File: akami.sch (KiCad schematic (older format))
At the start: 66 parts, among them J1 USB_C_Receptacle_USB2.0, J2 Conn_01x01, J3 Conn_01x01, Q2 AO3401A, U1 nRF52840, U2 TP4054, U3 AP2112K-3.3, U4 ProMicro_2, Y1 32MHz, Y2 32.768 kHz

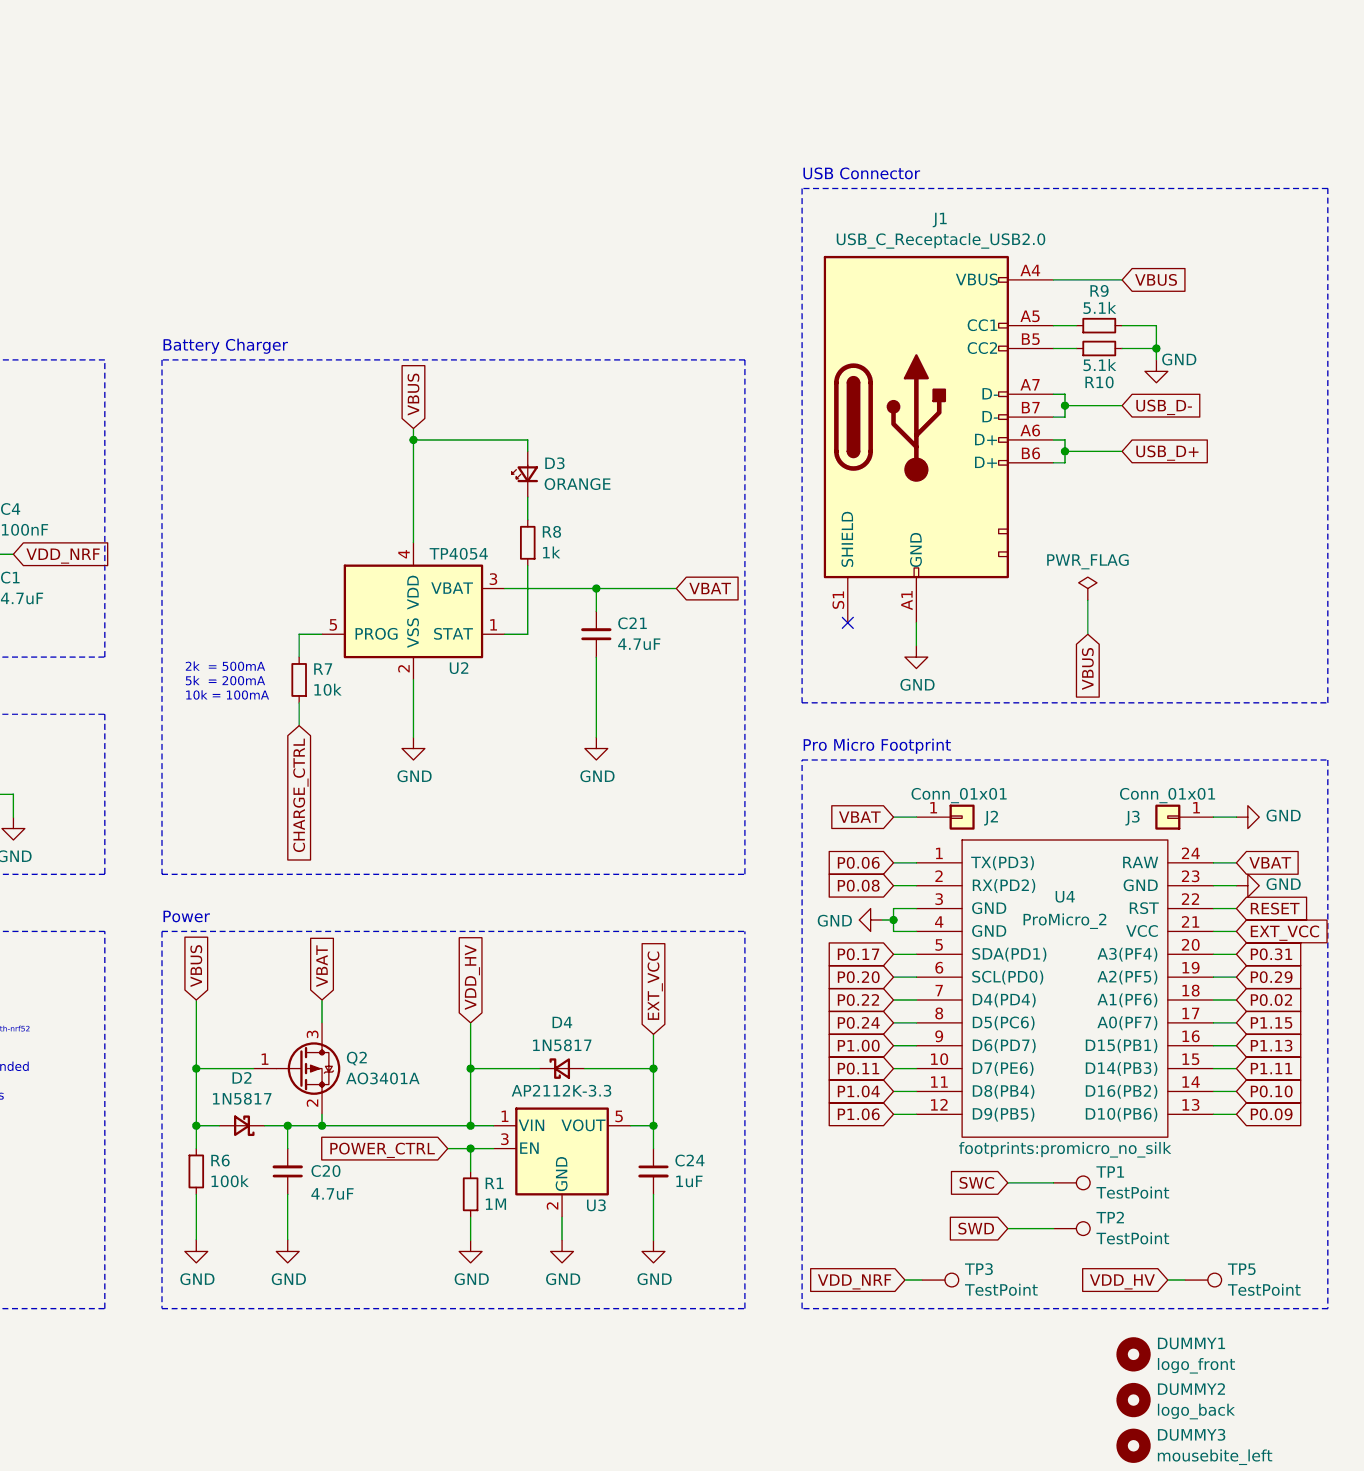
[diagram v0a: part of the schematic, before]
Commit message: rev 2.1 (hv): 1. remove the 1M pulldown on the LDO enable pin; AP2112K has an    internal pull-down already. 2. adjust pcb layout/routing slightly.
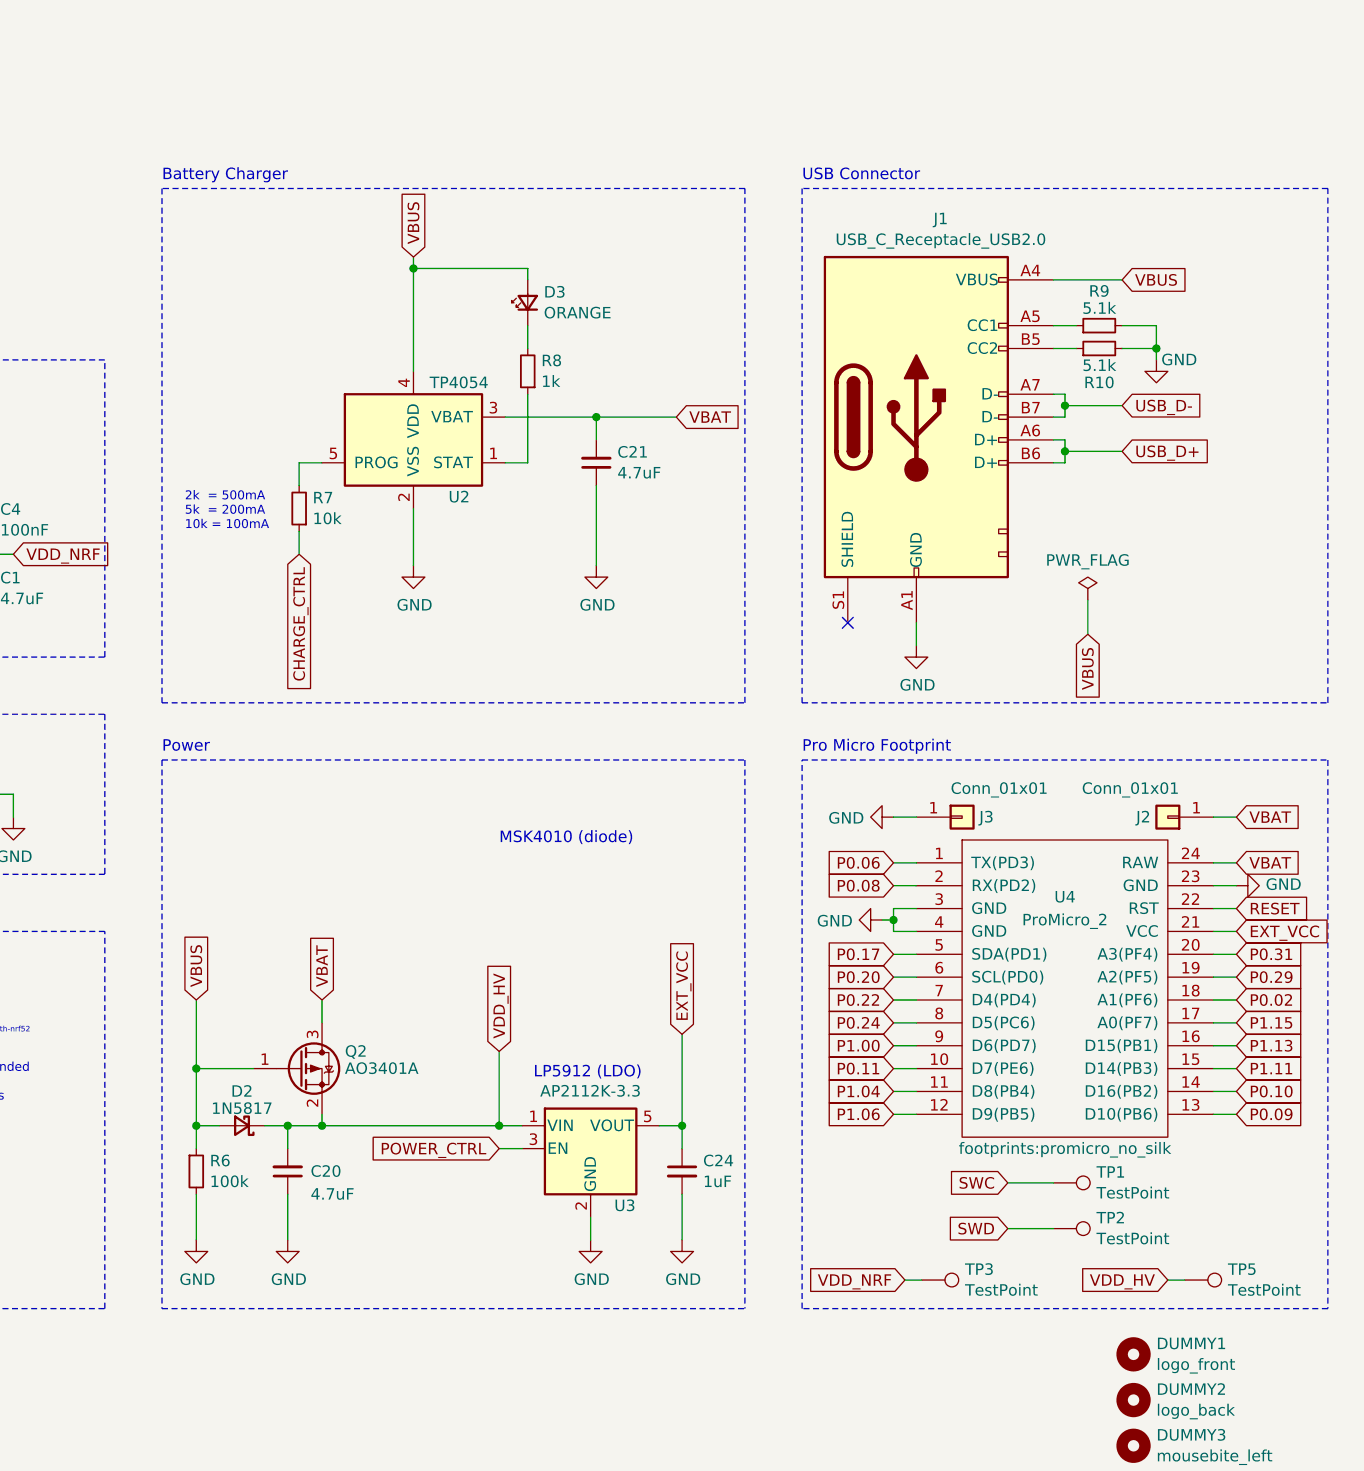
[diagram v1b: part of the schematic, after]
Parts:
- removed D4: 1N5817, Diode_SMD:D_SOD-323, symbol Device:D_Schottky_Small
- removed R1: 1M, Resistor_SMD:R_0402_1005Metric, symbol Device:R_Small
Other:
- note added: "LP5912 (LDO)"
- note added: "MSK4010 (diode)"
- moved on the sheet: C21, C24, D3, J2, J3, R7, R8, U2, U3

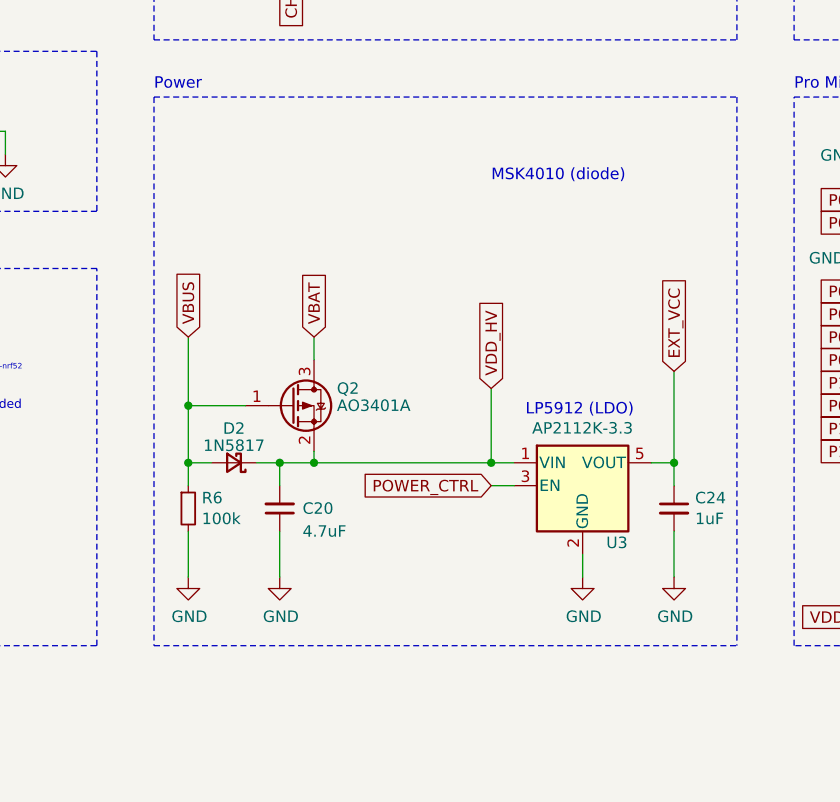
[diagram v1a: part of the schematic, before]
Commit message: rev 2.3 (hv): 1. replace AP2112 LDO with LP5912; it's some weird SMD package but    it's only 2x2mm; 500mA max output and 30uA quiescent. it's not    like we'll be the ones soldering it anyway.
2. similarly, replace 1N5817 schottkys with MSK4010 schottkys; it's
   SOD-523, so even smaller than the 323s.

3. move the components at the top a little further away from the
   USB port, since that has to be hand-soldered.

that freed up a bunch of space to hopefully try some stuff with the
power path.

note: gerbers/BOM/PnP files not updated
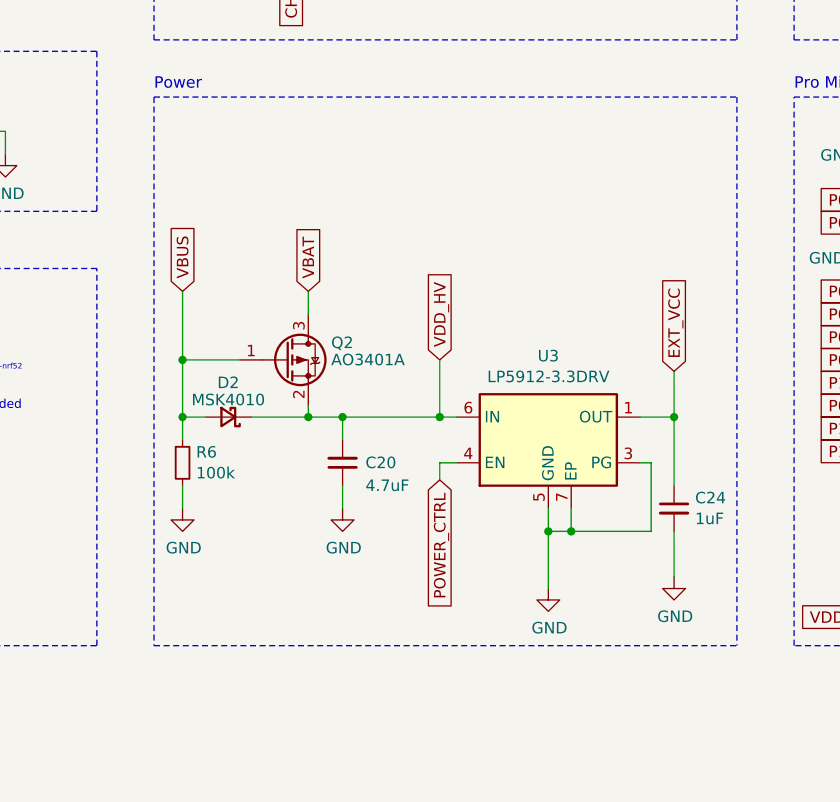
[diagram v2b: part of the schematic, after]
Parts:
- removed U3: AP2112K-3.3, Package_TO_SOT_SMD:SOT-23-5, symbol Regulator_Linear:AP2112K-3.3
- added U3: LP5912-3.3DRV, Package_SON:WSON-6-1EP_2x2mm_P0.65mm_EP1x1.6mm_ThermalVias, symbol Regulator_Linear:LP5912-3.3DRV
- D2: value 1N5817 -> MSK4010; footprint Diode_SMD:D_SOD-323 -> Diode_SMD:D_SOD-523; LCSC Part C489146 -> C345958
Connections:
- net EXT_VCC: now also U3.1 (OUT)
- net GND: now also U3.3 (PG), U3.5 (GND), U3.7 (EP)
- net POWER_CTRL: now also U3.4 (EN)
- net VDD_HV: now also U3.6 (IN)
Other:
- note removed: "LP5912 (LDO)"
- note removed: "MSK4010 (diode)"
- moved on the sheet: C20, D2, Q2, R6
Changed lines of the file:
@@
 Wire Wire Line
 	9350 5500 9450 5500
-Text GLabel 10550 6400 1    50   Input ~ 0
+Text GLabel 10525 6200 1    50   Input ~ 0
 VBUS
 $Comp
 L Device:R_Small R6
 U 1 1 60073401
-P 10550 7150
-F 0 "R6" H 10609 7196 50  0000 L CNN
-F 1 "100k" H 10609 7105 50  0000 L CNN
-F 2 "Resistor_SMD:R_0402_1005Metric" H 10550 7150 50  0001 C CNN
-F 3 "~" H 10550 7150 50  0001 C CNN
-F 4 "C25741" H 10550 7150 50  0001 C CNN "LCSC Part"
-	1    10550 7150
-	1    0    0    -1
-$EndComp
-Wire Wire Line
-	10550 7250 10550 7450
-Text GLabel 11100 6400 1    50   Input ~ 0
+P 10525 6950
+F 0 "R6" H 10584 6996 50  0000 L CNN
+F 1 "100k" H 10584 6905 50  0000 L CNN
+F 2 "Resistor_SMD:R_0402_1005Metric" H 10525 6950 50  0001 C CNN
+F 3 "~" H 10525 6950 50  0001 C CNN
+F 4 "C25741" H 10525 6950 50  0001 C CNN "LCSC Part"
+	1    10525 6950
+	1    0    0    -1
+$EndComp
+Wire Wire Line
+	10525 7050 10525 7150
+Text GLabel 11075 6200 1    50   Input ~ 0
 VBAT
 Wire Wire Line
-	11100 6400 11100 6500
-Wire Wire Line
-	10550 6700 10550 6950
-Wire Wire Line
-	10550 6950 10650 6950
-Connection ~ 10550 6950
-Wire Wire Line
-	10550 6950 10550 7050
+	11075 6200 11075 6300
+Wire Wire Line
+	10525 6500 10525 6750
+Wire Wire Line
+	10525 6750 10625 6750
+Connection ~ 10525 6750
+Wire Wire Line
+	10525 6750 10525 6850
 $Comp
 L Transistor_FET:IRLML9301 Q2
 U 1 1 60065EE0
-P 11000 6700
-F 0 "Q2" H 11200 6775 50  0000 L CNN
-F 1 "AO3401A" H 11200 6700 50  0000 L CNN
-F 2 "Package_TO_SOT_SMD:SOT-23" H 11200 6625 50  0001 L CIN
-F 3 "" H 11000 6700 50  0001 L CNN
-F 4 "C15127" H 11000 6700 50  0001 C CNN "LCSC Part"
-	1    11000 6700
-	1    0    0    -1
-$EndComp
-Wire Wire Line
-	11100 6900 11100 6950
+P 10975 6500
+F 0 "Q2" H 11175 6575 50  0000 L CNN
+F 1 "AO3401A" H 11175 6500 50  0000 L CNN
+F 2 "Package_TO_SOT_SMD:SOT-23" H 11175 6425 50  0001 L CIN
+F 3 "" H 10975 6500 50  0001 L CNN
+F 4 "C15127" H 10975 6500 50  0001 C CNN "LCSC Part"
+	1    10975 6500
+	1    0    0    -1
+$EndComp
+Wire Wire Line
+	11075 6700 11075 6750
 $Comp
 L akami:USB_C_Receptacle_USB2.0 J1
@@
 L power:GND #PWR0114
 U 1 1 6062C433
-P 10550 7450
-F 0 "#PWR0114" H 10550 7200 50  0001 C CNN
-F 1 "GND" H 10555 7277 50  0000 C CNN
-F 2 "" H 10550 7450 50  0001 C CNN
-F 3 "" H 10550 7450 50  0001 C CNN
-	1    10550 7450
+P 10525 7150
+F 0 "#PWR0114" H 10525 6900 50  0001 C CNN
+F 1 "GND" H 10530 6977 50  0000 C CNN
+F 2 "" H 10525 7150 50  0001 C CNN
+F 3 "" H 10525 7150 50  0001 C CNN
+	1    10525 7150
 	1    0    0    -1
 $EndComp
@@
 L power:GND #PWR0115
 U 1 1 6062D152
-P 10950 7450
-F 0 "#PWR0115" H 10950 7200 50  0001 C CNN
-F 1 "GND" H 10955 7277 50  0000 C CNN
-F 2 "" H 10950 7450 50  0001 C CNN
-F 3 "" H 10950 7450 50  0001 C CNN
-	1    10950 7450
+P 11225 7150
+F 0 "#PWR0115" H 11225 6900 50  0001 C CNN
+F 1 "GND" H 11230 6977 50  0000 C CNN
+F 2 "" H 11225 7150 50  0001 C CNN
+F 3 "" H 11225 7150 50  0001 C CNN
+	1    11225 7150
 	1    0    0    -1
 $EndComp
@@
 	1    0    0    -1
 $EndComp
-Wire Wire Line
-	10850 6950 10950 6950
-Wire Wire Line
-	10950 6950 10950 7050
-Connection ~ 10950 6950
-Wire Wire Line
-	10950 6950 11100 6950
-Wire Wire Line
-	10950 7250 10950 7450
 $Comp
 L Device:L_Small L2
@@
 	5200 2700 5200 3150
 $Comp
-L Regulator_Linear:AP2112K-3.3 U3
-U 1 1 6005829A
-P 12275 7050
-F 0 "U3" H 12425 6800 50  0000 C CNN
-F 1 "AP2112K-3.3" H 12275 7301 50  0000 C CNN
-F 2 "Package_TO_SOT_SMD:SOT-23-5" H 12275 7375 50  0001 C CNN
-F 3 "https://www.diodes.com/assets/Datasheets/AP2112.pdf" H 12275 7150 50  0001 C CNN
-F 4 "C51118" H 12275 7050 50  0001 C CNN "LCSC Part"
-	1    12275 7050
-	1    0    0    -1
-$EndComp
-Wire Wire Line
-	12575 6950 12675 6950
-Wire Wire Line
-	12275 7350 12275 7450
-$Comp
 L power:GND #PWR04
 U 1 1 603D3761
-P 12275 7450
-F 0 "#PWR04" H 12275 7200 50  0001 C CNN
-F 1 "GND" H 12280 7277 50  0000 C CNN
-F 2 "" H 12275 7450 50  0001 C CNN
-F 3 "" H 12275 7450 50  0001 C CNN
-	1    12275 7450
-	1    0    0    -1
-$EndComp
-Text GLabel 11875 7050 0    50   Input ~ 0
+P 12125 7500
+F 0 "#PWR04" H 12125 7250 50  0001 C CNN
+F 1 "GND" H 12130 7327 50  0000 C CNN
+F 2 "" H 12125 7500 50  0001 C CNN
+F 3 "" H 12125 7500 50  0001 C CNN
+	1    12125 7500
+	1    0    0    -1
+$EndComp
+Text GLabel 11650 7025 3    50   Input ~ 0
 POWER_CTRL
 Text GLabel 12675 6550 1    50   Input ~ 0
 EXT_VCC
-Text GLabel 11875 6625 1    50   Input ~ 0
+Text GLabel 11650 6500 1    50   Input ~ 0
 VDD_HV
 $Comp
 L Device:C_Small C20
 U 1 1 600BD765
-P 10950 7150
-F 0 "C20" H 10850 7150 50  0000 R CNN
-F 1 "4.7uF" H 10850 7250 50  0000 R CNN
-F 2 "Capacitor_SMD:C_0603_1608Metric" H 10950 7150 50  0001 C CNN
-F 3 "~" H 10950 7150 50  0001 C CNN
-F 4 "C19666" H 10950 7150 50  0001 C CNN "LCSC Part"
-	1    10950 7150
+P 11225 6950
+F 0 "C20" H 11125 6950 50  0000 R CNN
+F 1 "4.7uF" H 11125 7050 50  0000 R CNN
+F 2 "Capacitor_SMD:C_0603_1608Metric" H 11225 6950 50  0001 C CNN
+F 3 "~" H 11225 6950 50  0001 C CNN
+F 4 "C19666" H 11225 6950 50  0001 C CNN "LCSC Part"
+	1    11225 6950
 	-1   0    0    1
 $EndComp
@@
 Wire Wire Line
 	12675 7250 12675 7450
-Wire Wire Line
-	12675 6950 12675 7050
-Connection ~ 12675 6950
 $Comp
 L Mechanical:MountingHole DUMMY3
@@
 Wire Wire Line
 	14875 7625 14800 7625
-Text Notes 12025 6750 0    50   ~ 0
-LP5912 (LDO)
 $Comp
 L Connector_Generic:Conn_01x01 J3
@@
 	-1   0    0    1
 $EndComp
-Text Notes 11875 5725 0    50   ~ 0
-MSK4010 (diode)
-Wire Wire Line
-	12675 6550 12675 6950
-Connection ~ 11100 6950
 $Comp
 L Device:D_Schottky_Small D2
 U 1 1 600A857A
-P 10750 6950
-F 0 "D2" H 10750 6800 50  0000 C CNN
-F 1 "1N5817" H 10750 6875 50  0000 C CNN
-F 2 "Diode_SMD:D_SOD-323" V 10750 6950 50  0001 C CNN
-F 3 "~" V 10750 6950 50  0001 C CNN
-F 4 "C489146" H 10750 6950 50  0001 C CNN "LCSC Part"
-	1    10750 6950
+P 10725 6750
+F 0 "D2" H 10725 6600 50  0000 C CNN
+F 1 "MSK4010" H 10725 6675 50  0000 C CNN
+F 2 "Diode_SMD:D_SOD-523" V 10725 6750 50  0001 C CNN
+F 3 "~" V 10725 6750 50  0001 C CNN
+F 4 "C345958" H 10725 6750 50  0001 C CNN "LCSC Part"
+	1    10725 6750
 	-1   0    0    1
 $EndComp
-Wire Wire Line
-	11875 6625 11875 6950
-Connection ~ 11875 6950
-Wire Wire Line
-	11875 6950 11975 6950
-Wire Wire Line
-	11875 7050 11975 7050
 Wire Notes Line
 	10400 5350 10400 7750
 Wire Notes Line
 	12950 5350 12950 7750
-Connection ~ 10550 6700
-Wire Wire Line
-	10550 6700 10800 6700
-Wire Wire Line
-	10550 6400 10550 6700
-Wire Wire Line
-	11100 6950 11875 6950
+Connection ~ 10525 6500
+Wire Wire Line
+	10525 6500 10775 6500
+Wire Wire Line
+	10525 6200 10525 6500
+$Comp
+L Regulator_Linear:LP5912-3.3DRV U3
+U 1 1 60D2A9A8
+P 12125 6850
+F 0 "U3" H 12125 7217 50  0000 C CNN
+F 1 "LP5912-3.3DRV" H 12125 7126 50  0000 C CNN
+F 2 "Package_SON:WSON-6-1EP_2x2mm_P0.65mm_EP1x1.6mm_ThermalVias" H 12125 7200 50  0001 C CNN
+F 3 "http://www.ti.com/lit/ds/symlink/lp5912.pdf" H 12125 7350 50  0001 C CNN
+F 4 "C134121" H 12125 6850 50  0001 C CNN "LCSC Part"
+	1    12125 6850
+	1    0    0    -1
+$EndComp
+Connection ~ 11075 6750
+Wire Wire Line
+	11075 6750 11225 6750
+Wire Wire Line
+	11650 6500 11650 6750
+Connection ~ 11650 6750
+Wire Wire Line
+	11650 6750 11725 6750
+Wire Wire Line
+	11650 7025 11650 6950
+Wire Wire Line
+	11650 6950 11725 6950
+Wire Wire Line
+	12675 6550 12675 6750
+Wire Wire Line
+	12525 6750 12675 6750
+Connection ~ 12675 6750
+Wire Wire Line
+	12675 6750 12675 7050
+Wire Wire Line
+	12525 6950 12575 6950
+Wire Wire Line
+	11225 6750 11225 6850
+Connection ~ 11225 6750
+Wire Wire Line
+	11225 6750 11650 6750
+Wire Wire Line
+	10825 6750 11075 6750
+Wire Wire Line
+	12125 7150 12125 7250
+Wire Wire Line
+	12225 7150 12225 7250
+Wire Wire Line
+	12225 7250 12125 7250
+Connection ~ 12125 7250
+Wire Wire Line
+	12125 7250 12125 7500
+Wire Wire Line
+	12225 7250 12575 7250
+Wire Wire Line
+	12575 7250 12575 6950
+Connection ~ 12225 7250
+Wire Wire Line
+	11225 7150 11225 7050
 $EndSCHEMATC
